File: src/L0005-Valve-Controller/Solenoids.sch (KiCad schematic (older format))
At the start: 41 parts, among them K1 AQH0223AX, K2 AQH0223AX, K3 AQH0223AX, K4 AQH0223AX, K5 AQH0223AX, K6 AQH0223AX, P3 647676-3, P4 647676-3, P5 647676-3, P6 647676-3, P7 647676-3, P8 647676-3

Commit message: routed solenoid SSRs
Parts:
- C16, C17, C18, C19, C20, C21: footprint (none) -> L0005-Valve-Controller:CAP_1206
- H1, H2, H3, H4: footprint (none) -> L0005-Valve-Controller:MountingHole_4.3mm_M4_DIN965
- K1, K2, K3, K4, K5, K6: footprint RELAY_AQH0223AX -> L0005-Valve-Controller:RELAY_AQH0223AX
- LOGO1: footprint (none) -> L0005-Valve-Controller:Logo
- P3, P4, P5, P6, P7, P8: footprint CONN_2043-1X04G00DAU_OUP -> L0005-Valve-Controller:353130360
- R10, R11, R12, R13, R2, R3, R4, R5, R6, R7, R8, R9: footprint (none) -> L0005-Valve-Controller:RES_0603
- RV1, RV2, RV3, RV4, RV5, RV6: footprint (none) -> L0005-Valve-Controller:PV275K4032R2
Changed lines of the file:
@@
 F 0 "R2" V 2129 2094 50  0000 L CNN
 F 1 "100" V 2220 2094 50  0000 L CNN
-F 2 "" H 2225 1525 50  0001 L BNN
+F 2 "L0005-Valve-Controller:RES_0603" H 2225 1525 50  0001 L BNN
 F 3 "" H 2175 2025 50  0001 L BNN
 	1    2175 2025
@@
 F 0 "K1" H 2650 1950 50  0000 C CNN
 F 1 "AQH0223AX" H 2650 1951 50  0001 C CNN
-F 2 "RELAY_AQH0223AX" H 2950 1075 50  0001 L BNN
+F 2 "L0005-Valve-Controller:RELAY_AQH0223AX" H 2950 1075 50  0001 L BNN
 F 3 "" H 2650 1575 50  0001 L BNN
 	1    2650 1575
@@
 F 0 "RV1" H 3300 1550 50  0000 L CNN
 F 1 "275V" H 3300 1450 50  0000 L CNN
-F 2 "" V 3155 1525 50  0001 C CNN
+F 2 "L0005-Valve-Controller:PV275K4032R2" V 3155 1525 50  0001 C CNN
 F 3 "~" H 3225 1525 50  0001 C CNN
 	1    3225 1525
@@
 F 0 "C16" V 3604 1628 50  0000 L CNN
 F 1 "0.1uF" V 3695 1628 50  0000 L CNN
-F 2 "" H 3550 1125 50  0001 L BNN
+F 2 "L0005-Valve-Controller:CAP_1206" H 3550 1125 50  0001 L BNN
 F 3 "" H 3600 1525 50  0001 L BNN
 	1    3650 1525
@@
 F 0 "P3" H 4850 1700 60  0000 L CNN
 F 1 "647676-3" H 5053 1372 60  0001 L CNN
-F 2 "CONN_2043-1X04G00DAU_OUP" H 4875 975 60  0001 C CNN
+F 2 "L0005-Valve-Controller:353130360" H 4875 975 60  0001 C CNN
 F 3 "" H 4525 1525 60  0001 C CNN
 	1    4525 1525
@@
 F 0 "R3" V 3604 1894 50  0000 L CNN
 F 1 "100" V 3695 1894 50  0000 L CNN
-F 2 "" H 3700 1325 50  0001 L BNN
+F 2 "L0005-Valve-Controller:RES_0603" H 3700 1325 50  0001 L BNN
 F 3 "" H 3650 1825 50  0001 L BNN
 	1    3650 1825
@@
 F 0 "R4" V 2104 3819 50  0000 L CNN
 F 1 "100" V 2195 3819 50  0000 L CNN
-F 2 "" H 2200 3250 50  0001 L BNN
+F 2 "L0005-Valve-Controller:RES_0603" H 2200 3250 50  0001 L BNN
 F 3 "" H 2150 3750 50  0001 L BNN
 	1    2150 3750
@@
 F 0 "K2" H 2625 3675 50  0000 C CNN
 F 1 "AQH0223AX" H 2625 3676 50  0001 C CNN
-F 2 "RELAY_AQH0223AX" H 2925 2800 50  0001 L BNN
+F 2 "L0005-Valve-Controller:RELAY_AQH0223AX" H 2925 2800 50  0001 L BNN
 F 3 "" H 2625 3300 50  0001 L BNN
 	1    2625 3300
@@
 F 0 "RV2" H 3275 3275 50  0000 L CNN
 F 1 "275V" H 3275 3175 50  0000 L CNN
-F 2 "" V 3130 3250 50  0001 C CNN
+F 2 "L0005-Valve-Controller:PV275K4032R2" V 3130 3250 50  0001 C CNN
 F 3 "~" H 3200 3250 50  0001 C CNN
 	1    3200 3250
@@
 F 0 "C17" V 3579 3353 50  0000 L CNN
 F 1 "0.1uF" V 3670 3353 50  0000 L CNN
-F 2 "" H 3525 2850 50  0001 L BNN
+F 2 "L0005-Valve-Controller:CAP_1206" H 3525 2850 50  0001 L BNN
 F 3 "" H 3575 3250 50  0001 L BNN
 	1    3625 3250
@@
 F 0 "P4" H 4825 3425 60  0000 L CNN
 F 1 "647676-3" H 5028 3097 60  0001 L CNN
-F 2 "CONN_2043-1X04G00DAU_OUP" H 4850 2700 60  0001 C CNN
+F 2 "L0005-Valve-Controller:353130360" H 4850 2700 60  0001 C CNN
 F 3 "" H 4500 3250 60  0001 C CNN
 	1    4500 3250
@@
 F 0 "R6" V 3579 3619 50  0000 L CNN
 F 1 "100" V 3670 3619 50  0000 L CNN
-F 2 "" H 3675 3050 50  0001 L BNN
+F 2 "L0005-Valve-Controller:RES_0603" H 3675 3050 50  0001 L BNN
 F 3 "" H 3625 3550 50  0001 L BNN
 	1    3625 3550
@@
 F 0 "R5" V 2104 5569 50  0000 L CNN
 F 1 "100" V 2195 5569 50  0000 L CNN
-F 2 "" H 2200 5000 50  0001 L BNN
+F 2 "L0005-Valve-Controller:RES_0603" H 2200 5000 50  0001 L BNN
 F 3 "" H 2150 5500 50  0001 L BNN
 	1    2150 5500
@@
 F 0 "K3" H 2625 5425 50  0000 C CNN
 F 1 "AQH0223AX" H 2625 5426 50  0001 C CNN
-F 2 "RELAY_AQH0223AX" H 2925 4550 50  0001 L BNN
+F 2 "L0005-Valve-Controller:RELAY_AQH0223AX" H 2925 4550 50  0001 L BNN
 F 3 "" H 2625 5050 50  0001 L BNN
 	1    2625 5050
@@
 F 0 "RV3" H 3275 5025 50  0000 L CNN
 F 1 "275V" H 3275 4925 50  0000 L CNN
-F 2 "" V 3130 5000 50  0001 C CNN
+F 2 "L0005-Valve-Controller:PV275K4032R2" V 3130 5000 50  0001 C CNN
 F 3 "~" H 3200 5000 50  0001 C CNN
 	1    3200 5000
@@
 F 0 "C18" V 3579 5103 50  0000 L CNN
 F 1 "0.1uF" V 3670 5103 50  0000 L CNN
-F 2 "" H 3525 4600 50  0001 L BNN
+F 2 "L0005-Valve-Controller:CAP_1206" H 3525 4600 50  0001 L BNN
 F 3 "" H 3575 5000 50  0001 L BNN
 	1    3625 5000
@@
 F 0 "P5" H 4825 5175 60  0000 L CNN
 F 1 "647676-3" H 5028 4847 60  0001 L CNN
-F 2 "CONN_2043-1X04G00DAU_OUP" H 4850 4450 60  0001 C CNN
+F 2 "L0005-Valve-Controller:353130360" H 4850 4450 60  0001 C CNN
 F 3 "" H 4500 5000 60  0001 C CNN
 	1    4500 5000
@@
 F 0 "R7" V 3579 5369 50  0000 L CNN
 F 1 "100" V 3670 5369 50  0000 L CNN
-F 2 "" H 3675 4800 50  0001 L BNN
+F 2 "L0005-Valve-Controller:RES_0603" H 3675 4800 50  0001 L BNN
 F 3 "" H 3625 5300 50  0001 L BNN
 	1    3625 5300
@@
 F 0 "R10" V 6554 2094 50  0000 L CNN
 F 1 "100" V 6645 2094 50  0000 L CNN
-F 2 "" H 6650 1525 50  0001 L BNN
+F 2 "L0005-Valve-Controller:RES_0603" H 6650 1525 50  0001 L BNN
 F 3 "" H 6600 2025 50  0001 L BNN
 	1    6600 2025
@@
 F 0 "K6" H 7075 1950 50  0000 C CNN
 F 1 "AQH0223AX" H 7075 1951 50  0001 C CNN
-F 2 "RELAY_AQH0223AX" H 7375 1075 50  0001 L BNN
+F 2 "L0005-Valve-Controller:RELAY_AQH0223AX" H 7375 1075 50  0001 L BNN
 F 3 "" H 7075 1575 50  0001 L BNN
 	1    7075 1575
@@
 F 0 "RV6" H 7725 1550 50  0000 L CNN
 F 1 "275V" H 7725 1450 50  0000 L CNN
-F 2 "" V 7580 1525 50  0001 C CNN
+F 2 "L0005-Valve-Controller:PV275K4032R2" V 7580 1525 50  0001 C CNN
 F 3 "~" H 7650 1525 50  0001 C CNN
 	1    7650 1525
@@
 F 0 "C21" V 8029 1628 50  0000 L CNN
 F 1 "0.1uF" V 8120 1628 50  0000 L CNN
-F 2 "" H 7975 1125 50  0001 L BNN
+F 2 "L0005-Valve-Controller:CAP_1206" H 7975 1125 50  0001 L BNN
 F 3 "" H 8025 1525 50  0001 L BNN
 	1    8075 1525
@@
 F 0 "P8" H 9275 1700 60  0000 L CNN
 F 1 "647676-3" H 9478 1372 60  0001 L CNN
-F 2 "CONN_2043-1X04G00DAU_OUP" H 9300 975 60  0001 C CNN
+F 2 "L0005-Valve-Controller:353130360" H 9300 975 60  0001 C CNN
 F 3 "" H 8950 1525 60  0001 C CNN
 	1    8950 1525
@@
 F 0 "R13" V 8029 1894 50  0000 L CNN
 F 1 "100" V 8120 1894 50  0000 L CNN
-F 2 "" H 8125 1325 50  0001 L BNN
+F 2 "L0005-Valve-Controller:RES_0603" H 8125 1325 50  0001 L BNN
 F 3 "" H 8075 1825 50  0001 L BNN
 	1    8075 1825
@@
 F 0 "R8" V 6529 3819 50  0000 L CNN
 F 1 "100" V 6620 3819 50  0000 L CNN
-F 2 "" H 6625 3250 50  0001 L BNN
+F 2 "L0005-Valve-Controller:RES_0603" H 6625 3250 50  0001 L BNN
 F 3 "" H 6575 3750 50  0001 L BNN
 	1    6575 3750
@@
 F 0 "K4" H 7050 3675 50  0000 C CNN
 F 1 "AQH0223AX" H 7050 3676 50  0001 C CNN
-F 2 "RELAY_AQH0223AX" H 7350 2800 50  0001 L BNN
+F 2 "L0005-Valve-Controller:RELAY_AQH0223AX" H 7350 2800 50  0001 L BNN
 F 3 "" H 7050 3300 50  0001 L BNN
 	1    7050 3300
@@
 F 0 "RV4" H 7700 3275 50  0000 L CNN
 F 1 "275V" H 7700 3175 50  0000 L CNN
-F 2 "" V 7555 3250 50  0001 C CNN
+F 2 "L0005-Valve-Controller:PV275K4032R2" V 7555 3250 50  0001 C CNN
 F 3 "~" H 7625 3250 50  0001 C CNN
 	1    7625 3250
@@
 F 0 "C19" V 8004 3353 50  0000 L CNN
 F 1 "0.1uF" V 8095 3353 50  0000 L CNN
-F 2 "" H 7950 2850 50  0001 L BNN
+F 2 "L0005-Valve-Controller:CAP_1206" H 7950 2850 50  0001 L BNN
 F 3 "" H 8000 3250 50  0001 L BNN
 	1    8050 3250
@@
 F 0 "P6" H 9250 3425 60  0000 L CNN
 F 1 "647676-3" H 9453 3097 60  0001 L CNN
-F 2 "CONN_2043-1X04G00DAU_OUP" H 9275 2700 60  0001 C CNN
+F 2 "L0005-Valve-Controller:353130360" H 9275 2700 60  0001 C CNN
 F 3 "" H 8925 3250 60  0001 C CNN
 	1    8925 3250
@@
 F 0 "R11" V 8004 3619 50  0000 L CNN
 F 1 "100" V 8095 3619 50  0000 L CNN
-F 2 "" H 8100 3050 50  0001 L BNN
+F 2 "L0005-Valve-Controller:RES_0603" H 8100 3050 50  0001 L BNN
 F 3 "" H 8050 3550 50  0001 L BNN
 	1    8050 3550
@@
 F 0 "R9" V 6529 5569 50  0000 L CNN
 F 1 "100" V 6620 5569 50  0000 L CNN
-F 2 "" H 6625 5000 50  0001 L BNN
+F 2 "L0005-Valve-Controller:RES_0603" H 6625 5000 50  0001 L BNN
 F 3 "" H 6575 5500 50  0001 L BNN
 	1    6575 5500
@@
 F 0 "K5" H 7050 5425 50  0000 C CNN
 F 1 "AQH0223AX" H 7050 5426 50  0001 C CNN
-F 2 "RELAY_AQH0223AX" H 7350 4550 50  0001 L BNN
+F 2 "L0005-Valve-Controller:RELAY_AQH0223AX" H 7350 4550 50  0001 L BNN
 F 3 "" H 7050 5050 50  0001 L BNN
 	1    7050 5050
@@
 F 0 "RV5" H 7700 5025 50  0000 L CNN
 F 1 "275V" H 7700 4925 50  0000 L CNN
-F 2 "" V 7555 5000 50  0001 C CNN
+F 2 "L0005-Valve-Controller:PV275K4032R2" V 7555 5000 50  0001 C CNN
 F 3 "~" H 7625 5000 50  0001 C CNN
 	1    7625 5000
@@
 F 0 "C20" V 8004 5103 50  0000 L CNN
 F 1 "0.1uF" V 8095 5103 50  0000 L CNN
-F 2 "" H 7950 4600 50  0001 L BNN
+F 2 "L0005-Valve-Controller:CAP_1206" H 7950 4600 50  0001 L BNN
 F 3 "" H 8000 5000 50  0001 L BNN
 	1    8050 5000
@@
 F 0 "P7" H 9250 5175 60  0000 L CNN
 F 1 "647676-3" H 9453 4847 60  0001 L CNN
-F 2 "CONN_2043-1X04G00DAU_OUP" H 9275 4450 60  0001 C CNN
+F 2 "L0005-Valve-Controller:353130360" H 9275 4450 60  0001 C CNN
 F 3 "" H 8925 5000 60  0001 C CNN
 	1    8925 5000
@@
 F 0 "R12" V 8004 5369 50  0000 L CNN
 F 1 "100" V 8095 5369 50  0000 L CNN
-F 2 "" H 8100 4800 50  0001 L BNN
+F 2 "L0005-Valve-Controller:RES_0603" H 8100 4800 50  0001 L BNN
 F 3 "" H 8050 5300 50  0001 L BNN
 	1    8050 5300
@@
 F 0 "LOGO1" H 2703 6621 50  0001 L CNN
 F 1 "Logo" H 2425 6825 50  0000 L CNN
-F 2 "" H 2525 6575 50  0001 C CNN
+F 2 "L0005-Valve-Controller:Logo" H 2525 6575 50  0001 C CNN
 F 3 "" H 2525 6575 50  0001 C CNN
 	1    2525 6575
@@
 F 0 "H2" H 2925 6800 50  0000 L CNN
 F 1 "Mounting-Hole" H 2725 6350 50  0000 L CNN
-F 2 "" H 2975 6575 50  0001 C CNN
+F 2 "L0005-Valve-Controller:MountingHole_4.3mm_M4_DIN965" H 2975 6575 50  0001 C CNN
 F 3 "" H 2975 6575 50  0001 C CNN
 	1    2975 6575
@@
 F 0 "H3" H 3575 6800 50  0000 L CNN
 F 1 "Mounting-Hole" H 3375 6350 50  0000 L CNN
-F 2 "" H 3625 6575 50  0001 C CNN
+F 2 "L0005-Valve-Controller:MountingHole_4.3mm_M4_DIN965" H 3625 6575 50  0001 C CNN
 F 3 "" H 3625 6575 50  0001 C CNN
 	1    3625 6575
@@
 F 0 "H1" H 2900 7375 50  0000 L CNN
 F 1 "Mounting-Hole" H 2700 6925 50  0000 L CNN
-F 2 "" H 2950 7150 50  0001 C CNN
+F 2 "L0005-Valve-Controller:MountingHole_4.3mm_M4_DIN965" H 2950 7150 50  0001 C CNN
 F 3 "" H 2950 7150 50  0001 C CNN
 	1    2950 7150
@@
 F 0 "H4" H 3575 7375 50  0000 L CNN
 F 1 "Mounting-Hole" H 3375 6925 50  0000 L CNN
-F 2 "" H 3625 7150 50  0001 C CNN
+F 2 "L0005-Valve-Controller:MountingHole_4.3mm_M4_DIN965" H 3625 7150 50  0001 C CNN
 F 3 "" H 3625 7150 50  0001 C CNN
 	1    3625 7150

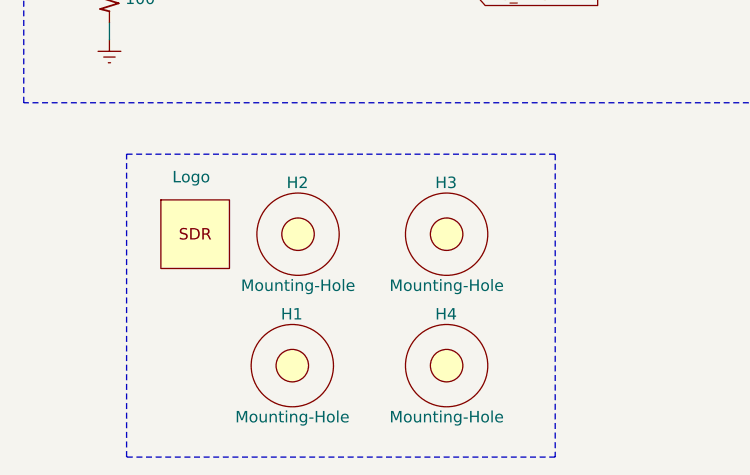
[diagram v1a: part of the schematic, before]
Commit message: finished controller routing
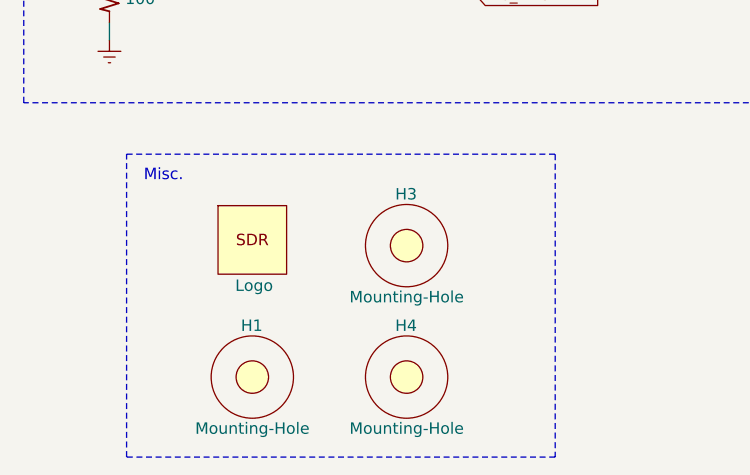
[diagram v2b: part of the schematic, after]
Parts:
- removed H2: Mounting-Hole, L0005-Valve-Controller:MountingHole_4.3mm_M4_DIN965, symbol L0005-Valve-Controller:Mounting-Hole
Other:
- note added: "Misc."
- moved on the sheet: H1, H3, H4
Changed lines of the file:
@@
 L L0005-Valve-Controller:Logo LOGO1
 U 1 1 62A36897
-P 2525 6575
-F 0 "LOGO1" H 2703 6621 50  0001 L CNN
-F 1 "Logo" H 2425 6825 50  0000 L CNN
-F 2 "L0005-Valve-Controller:Logo" H 2525 6575 50  0001 C CNN
-F 3 "" H 2525 6575 50  0001 C CNN
-	1    2525 6575
-	1    0    0    -1
-$EndComp
-$Comp
-L L0005-Valve-Controller:Mounting-Hole H2
-U 1 1 62A393A7
-P 2975 6575
-F 0 "H2" H 2925 6800 50  0000 L CNN
-F 1 "Mounting-Hole" H 2725 6350 50  0000 L CNN
-F 2 "L0005-Valve-Controller:MountingHole_4.3mm_M4_DIN965" H 2975 6575 50  0001 C CNN
-F 3 "" H 2975 6575 50  0001 C CNN
-	1    2975 6575
+P 2775 6600
+F 0 "LOGO1" H 2953 6646 50  0001 L CNN
+F 1 "Logo" H 2700 6400 50  0000 L CNN
+F 2 "L0005-Valve-Controller:Logo" H 2775 6600 50  0001 C CNN
+F 3 "" H 2775 6600 50  0001 C CNN
+	1    2775 6600
 	1    0    0    -1
 $EndComp
@@
 L L0005-Valve-Controller:Mounting-Hole H3
 U 1 1 62A3F7E0
-P 3625 6575
-F 0 "H3" H 3575 6800 50  0000 L CNN
-F 1 "Mounting-Hole" H 3375 6350 50  0000 L CNN
-F 2 "L0005-Valve-Controller:MountingHole_4.3mm_M4_DIN965" H 3625 6575 50  0001 C CNN
-F 3 "" H 3625 6575 50  0001 C CNN
-	1    3625 6575
+P 3450 6625
+F 0 "H3" H 3400 6850 50  0000 L CNN
+F 1 "Mounting-Hole" H 3200 6400 50  0000 L CNN
+F 2 "L0005-Valve-Controller:MountingHole_4.3mm_M4_DIN965" H 3450 6625 50  0001 C CNN
+F 3 "" H 3450 6625 50  0001 C CNN
+	1    3450 6625
 	1    0    0    -1
 $EndComp
@@
 L L0005-Valve-Controller:Mounting-Hole H1
 U 1 1 62A3FA12
-P 2950 7150
-F 0 "H1" H 2900 7375 50  0000 L CNN
-F 1 "Mounting-Hole" H 2700 6925 50  0000 L CNN
-F 2 "L0005-Valve-Controller:MountingHole_4.3mm_M4_DIN965" H 2950 7150 50  0001 C CNN
-F 3 "" H 2950 7150 50  0001 C CNN
-	1    2950 7150
+P 2775 7200
+F 0 "H1" H 2725 7425 50  0000 L CNN
+F 1 "Mounting-Hole" H 2525 6975 50  0000 L CNN
+F 2 "L0005-Valve-Controller:MountingHole_4.3mm_M4_DIN965" H 2775 7200 50  0001 C CNN
+F 3 "" H 2775 7200 50  0001 C CNN
+	1    2775 7200
 	1    0    0    -1
 $EndComp
@@
 L L0005-Valve-Controller:Mounting-Hole H4
 U 1 1 62A4004E
-P 3625 7150
-F 0 "H4" H 3575 7375 50  0000 L CNN
-F 1 "Mounting-Hole" H 3375 6925 50  0000 L CNN
-F 2 "L0005-Valve-Controller:MountingHole_4.3mm_M4_DIN965" H 3625 7150 50  0001 C CNN
-F 3 "" H 3625 7150 50  0001 C CNN
-	1    3625 7150
+P 3450 7200
+F 0 "H4" H 3400 7425 50  0000 L CNN
+F 1 "Mounting-Hole" H 3200 6975 50  0000 L CNN
+F 2 "L0005-Valve-Controller:MountingHole_4.3mm_M4_DIN965" H 3450 7200 50  0001 C CNN
+F 3 "" H 3450 7200 50  0001 C CNN
+	1    3450 7200
 	1    0    0    -1
 $EndComp
@@
 Wire Notes Line
 	2225 7550 2225 6225
+Text Notes 2300 6350 0    50   ~ 0
+Misc.
 $EndSCHEMATC
